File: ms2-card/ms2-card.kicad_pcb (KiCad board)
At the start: 2 copper layers, 100 x 54 mm, 30 parts, among them J10 MicroSD_SPI_CD, J11 I2C, J20 Smartcard Connector, J21 Card Edge, J22 Card Edge, J23 Conn_01x04, J30 Power_Only, M1 PI_PICO_ZERO, Q30 BC847, SW1 SW_Push, U1 W25Q128JVS

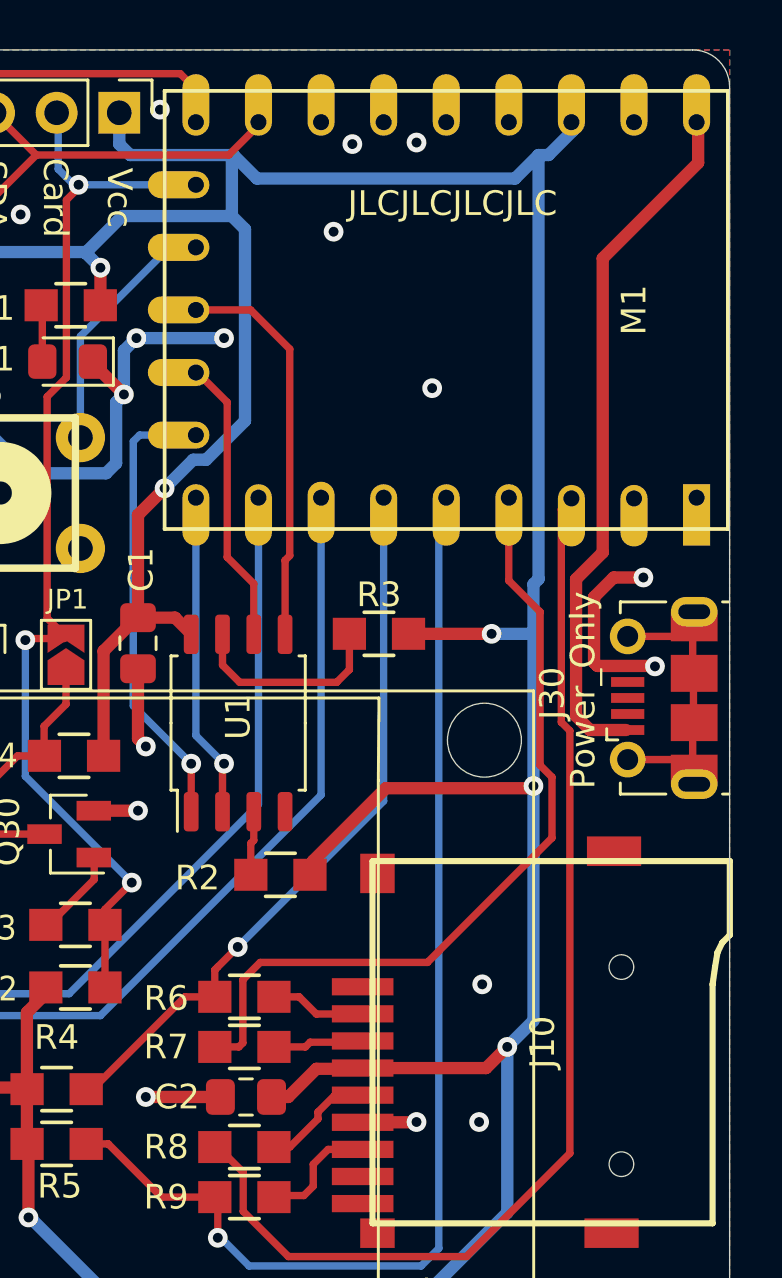
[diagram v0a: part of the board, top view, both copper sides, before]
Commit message: use larger holes
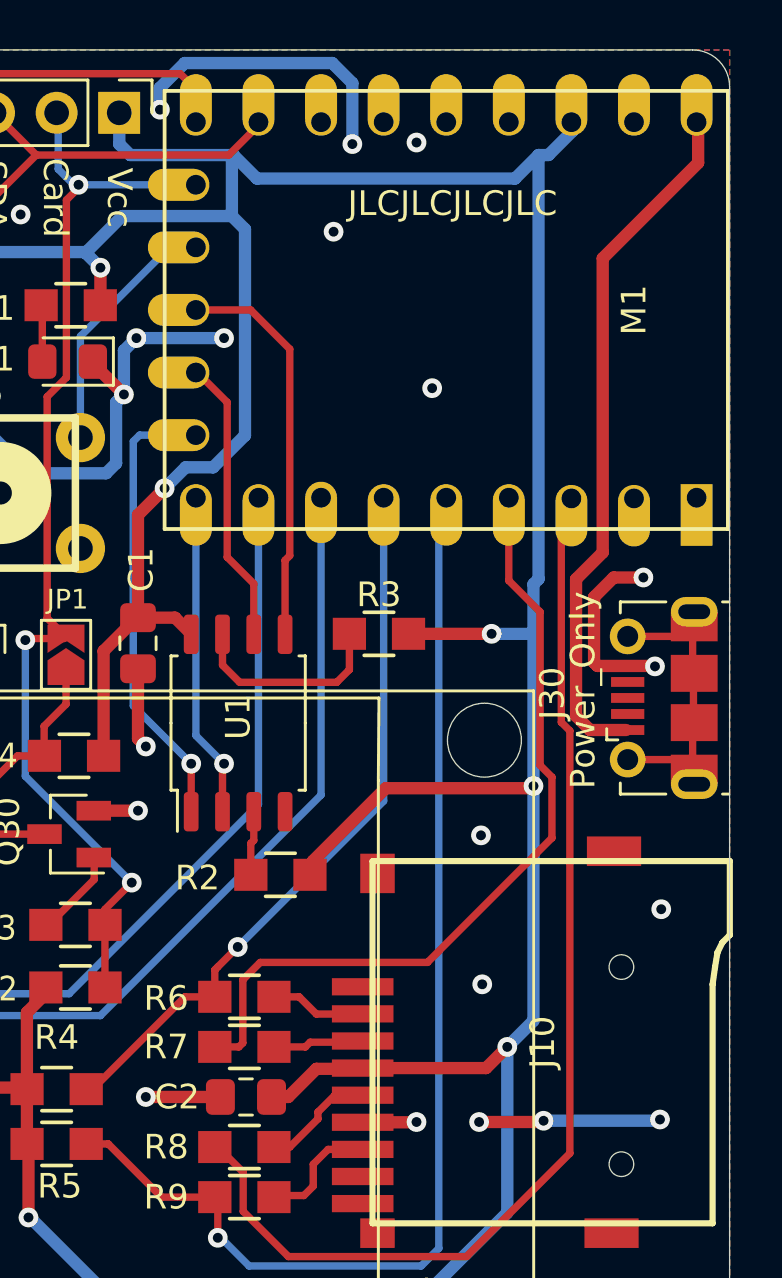
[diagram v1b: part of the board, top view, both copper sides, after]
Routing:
- net GND: track 36.2 -> 55.5 mm, vias 15 -> 21
- net (no net): vias 4 -> 2

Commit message: try to solve conflict
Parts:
- removed M1: PI_PICO_ZERO, Lokkarten:PI_PICO_ZERO
- removed Q30: BC847, Package_TO_SOT_SMD:SOT-23
- removed R22, R23: 1k, Resistors_SMD:R_0805_HandSolderingII
- removed R24: 100k, Resistors_SMD:R_0805_HandSolderingII
- added U1: RP2040, RP2040:RP2040-QFN-56, F.Cu at (185.8, 112.7)
- J11: value I2C -> Conn_01x06; footprint Connector_PinHeader_2.54mm:PinHeader_1x05_P2.54mm_Vertical -> Connector_PinHeader_2.54mm:PinHeader_1x06_P2.54mm_Vertical
- R6, R7: footprint Resistors_SMD:R_0805_HandSolderingII -> Resistor_SMD:R_0603_1608Metric_Pad0.98x0.95mm_HandSolder
- moved C1 22.8 mm to (183.0, 103.2)
- moved R3 17.8 mm to (180.1, 106.3), turned to 0 degrees
- moved U2 14.5 mm to (178.1, 112.8)
- moved R2 14.4 mm to (177.9, 119.2), turned to 0 degrees
- moved J11 2.57 mm to (175.8, 102.6)
- renumbered U1 to U2
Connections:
- J11 pad 2: /Card -> /MS2Power
- J11 pad 3: /SDA0 -> /Card
- J11 pad 4: /SCL0 -> /SDA0
- J11 pad 5: GND -> /SCL0
- J20 pad 1: Net-(J20-Pad1) -> /MS2Power
- J21 pad 1: Net-(J21-Pad1) -> /Card
- J21 pad 2: Net-(J21-Pad1) -> /Card
- J22 pad 1: Net-(J21-Pad1) -> /Card
- J22 pad 2: Net-(J21-Pad1) -> /Card
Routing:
- net VCC: track 180.0 -> 0.00 mm, vias 7 -> 0
- net Net-(J21-Pad1): track 134.4 -> 0.00 mm
- net /SCL0: track 94.7 -> 0.00 mm, vias 1 -> 0
- net /SDA0: track 81.6 -> 0.00 mm, vias 1 -> 0
- net Net-(J20-Pad2): track 70.3 -> 0.00 mm, vias 2 -> 0
- net Net-(J20-Pad4): track 56.0 -> 0.00 mm, vias 2 -> 0
- net GND: track 55.5 -> 0.00 mm, vias 21 -> 0
- net Net-(J20-Pad7): track 51.9 -> 0.00 mm
- net Net-(J20-Pad5): track 49.2 -> 0.00 mm, vias 2 -> 0
- net /MISO0: track 48.2 -> 0.00 mm, vias 1 -> 0
- net /CLK0: track 45.6 -> 0.00 mm
- net /Card: track 45.3 -> 0.00 mm, vias 3 -> 0
- net /SDA1: track 36.3 -> 0.00 mm, vias 1 -> 0
- net /MOSI0: track 33.5 -> 0.00 mm
- net /SCL1: track 30.7 -> 0.00 mm
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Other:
- net class Default removed
- net class Power removed
- board text added: "Lokkarten Emulator Gerhard Bertelsmann Hardi Stengelin 05/2022"
- board text removed: "Lokkarten Emulator Gerhard Bertelsmann Hardi Stengelin 03/2022"
